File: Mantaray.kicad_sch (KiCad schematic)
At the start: 0 parts

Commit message: External I/O
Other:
- sheet AUDIO OUT ports: added AUDIO_L_OUT, AUDIO_R_OUT, {I2S}; removed none
- sheet External Connectors ports: added AUDIO_L_OUT, AUDIO_R_OUT, AV_MODE0, AV_MODE1, AV_MODE2, EXPPORT_PORT1{USB}, EXPPORT_PORT2{USB}, EXPPORT_PORT3{USB}, EXPPORT_PORT4{USB}, SCART_RGB, SPDIF_OUT, VID_DACA, VID_DACB, VID_DACC, VID_DACD, VID_HSYNC, VID_VSYNC, WSS_CNTL0, WSS_CNTL1, {ETHERNET}, {HDMI}; removed none
- note added: "TODO: - Power Delivery - Audio Out - NAND/eMMC - Replace generic components with real part numbers"
- note removed: "TODO: - Power Delivery - Audio Out - NAND/eMMC - Replace generic components with real part numbers - Also memory i forgot"

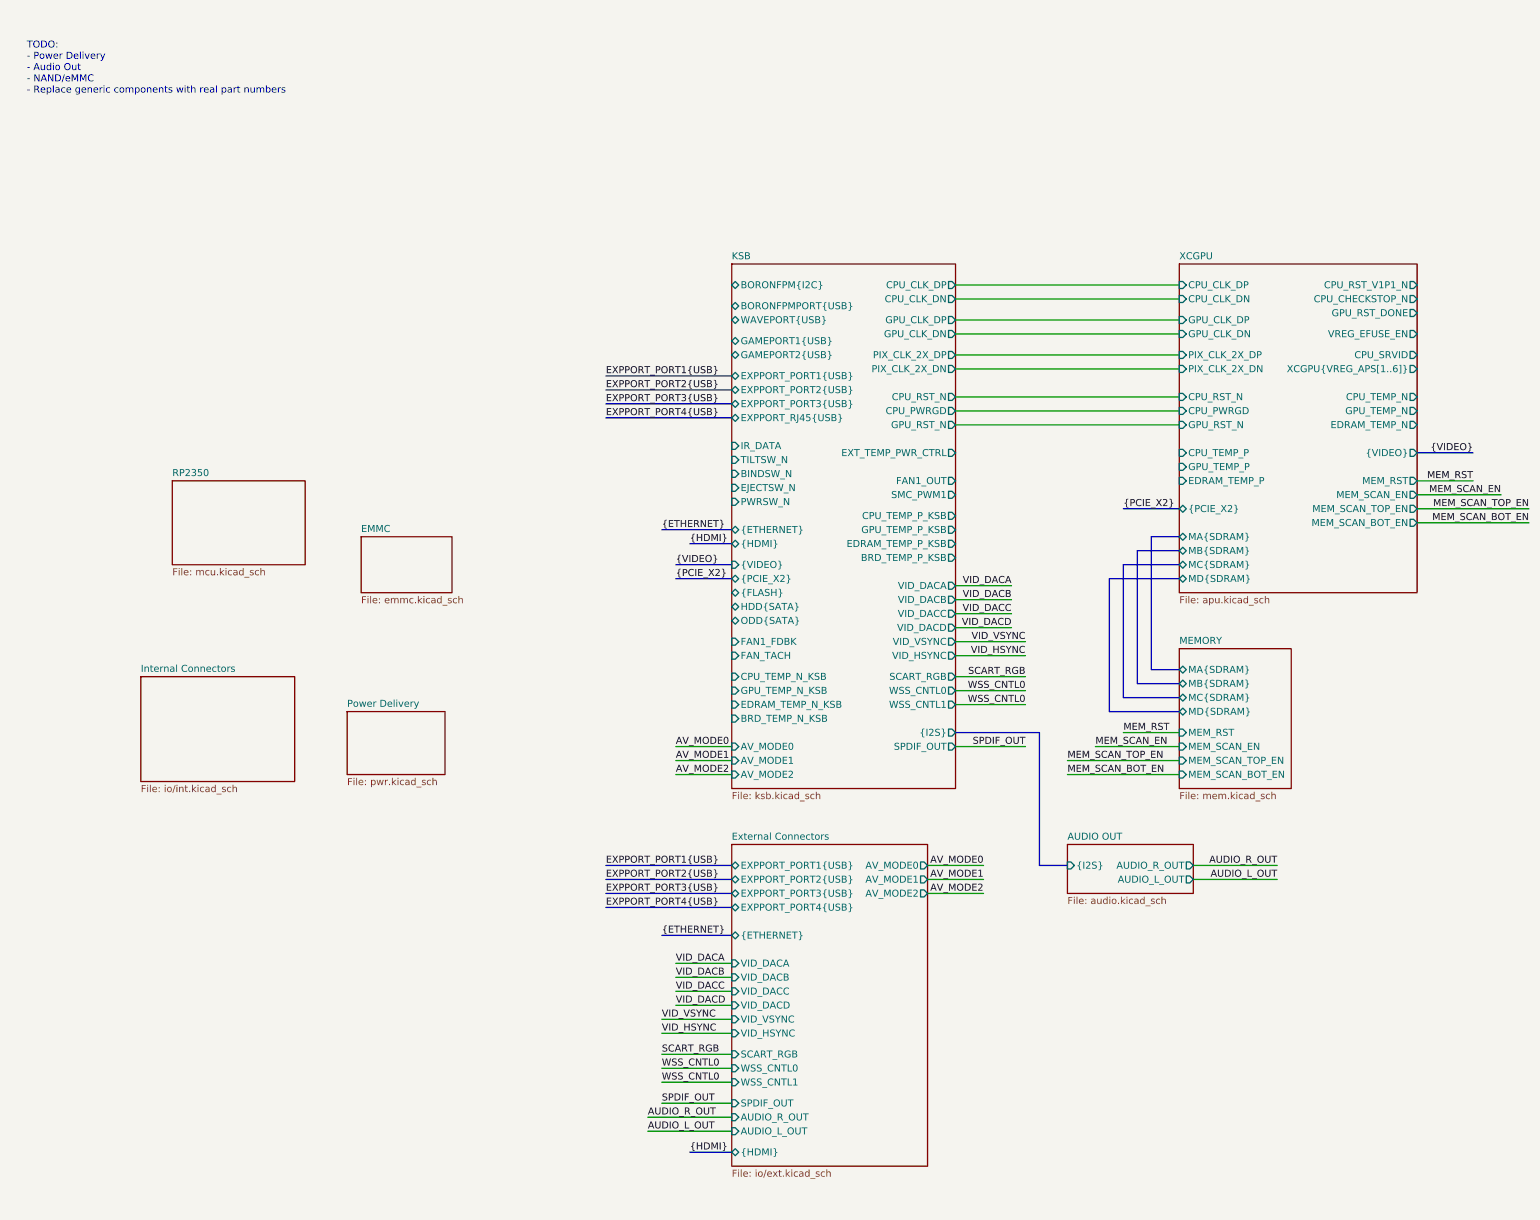
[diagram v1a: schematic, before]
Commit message: Cleanup, SMC GPIO connections and Temperature sensing
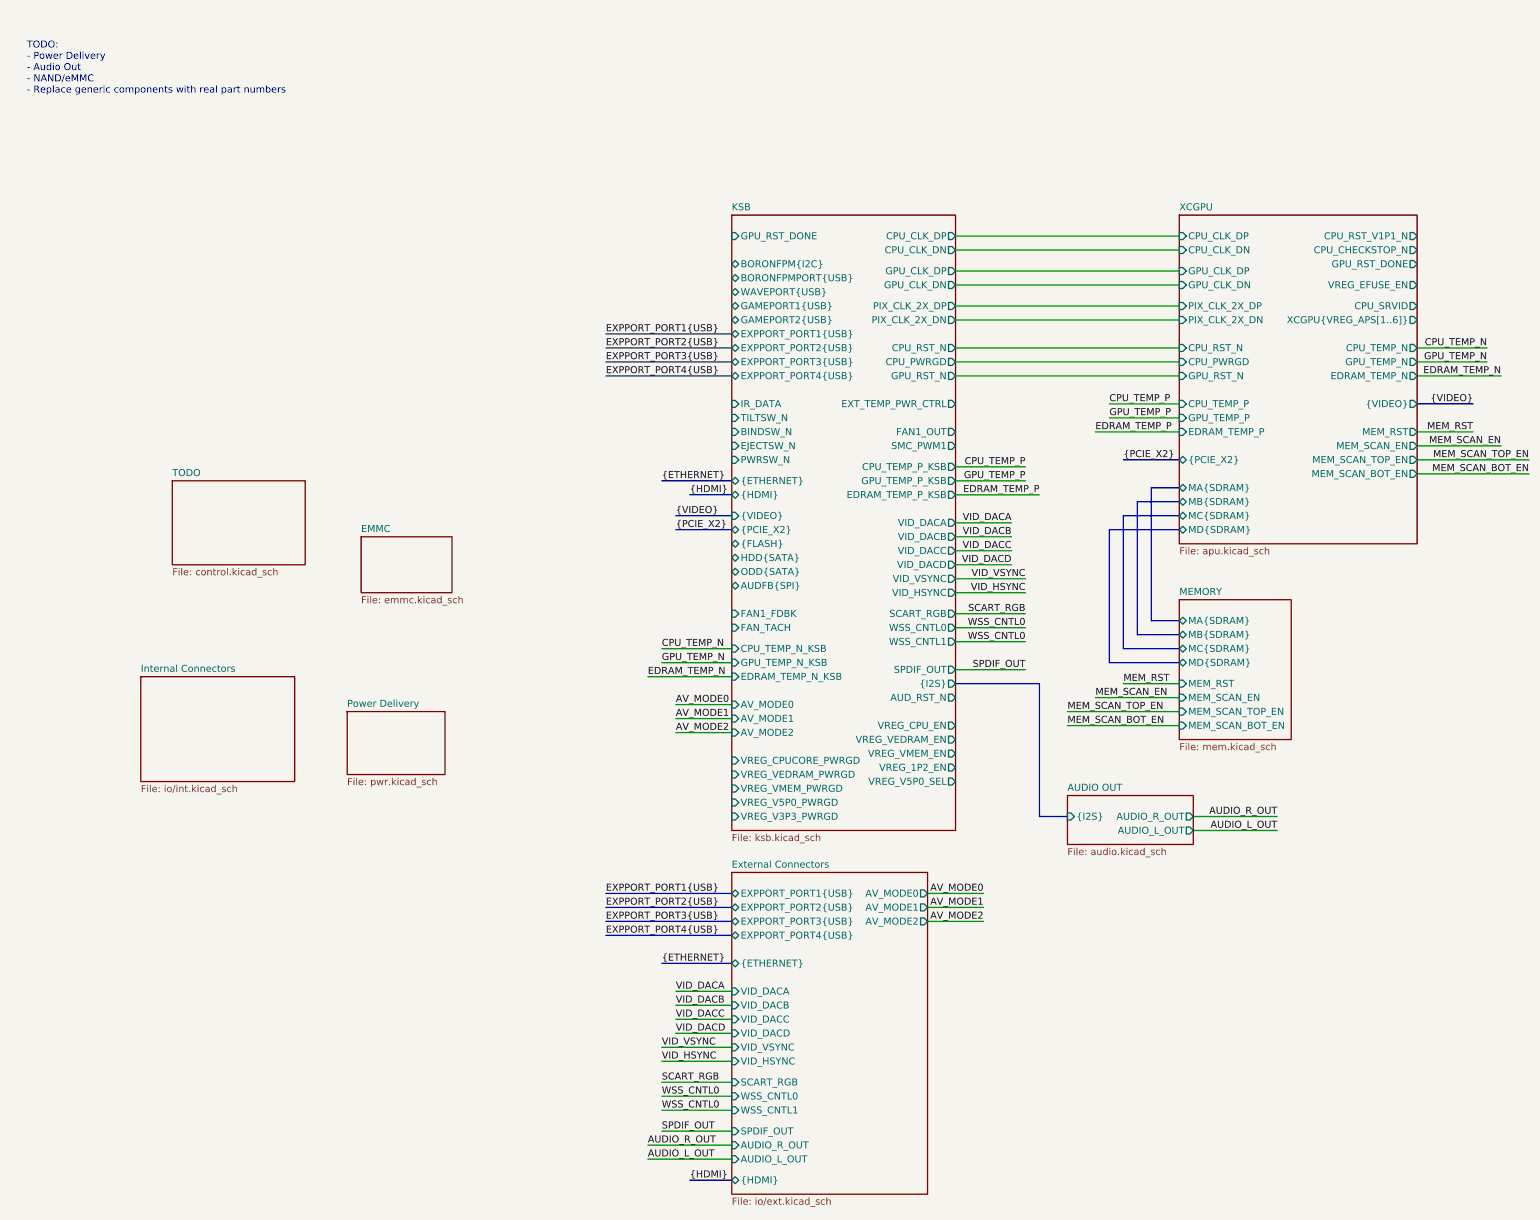
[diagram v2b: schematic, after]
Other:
- sheet RP2350 renamed TODO
- sheet KSB ports: added AUDFB{SPI}, AUD_RST_N, EXPPORT_PORT4{USB}, GPU_RST_DONE, VREG_1P2_EN, VREG_CPUCORE_PWRGD, VREG_CPU_EN, VREG_V3P3_PWRGD, VREG_V5P0_PWRGD, VREG_V5P0_SEL, VREG_VEDRAM_EN, VREG_VEDRAM_PWRGD, VREG_VMEM_EN, VREG_VMEM_PWRGD; removed BRD_TEMP_N_KSB, BRD_TEMP_P_KSB, EXPPORT_RJ45{USB}
- sheet TODO: file mcu.kicad_sch -> control.kicad_sch

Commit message: Internal Connectors
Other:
- sheet External Connectors ports: added EXPPORT_PORT0{USB}; removed EXPPORT_PORT4{USB}
- sheet Internal Connectors ports: added BINDSW_N, BORONFPMPORT{USB}, BORONFPM{I2C}, EJECTSW_N, FAN1_FDBK, FAN1_OUT, FAN_TACH, GAMEPORT1{USB}, GAMEPORT2{USB}, IR_DATA, PWRSW_N, SMC_PWM1, SPKR_DRIVE_N, SPKR_DRIVE_P, TILTSW_N, TRAY_OPEN, TRAY_STATUS; removed none
- sheet KSB ports: added EXPPORT_PORT0{USB}, TRAY_OPEN, TRAY_STATUS; removed EXPPORT_PORT4{USB}, EXT_TEMP_PWR_CTRL

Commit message: Cleanup & Debug I/O
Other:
- sheet EMMC renamed FLASH
- removed sheet TODO
- sheet AUDIO OUT ports: added AUD_RST_N; removed none
- sheet FLASH: file emmc.kicad_sch -> flash.kicad_sch
- sheet FLASH ports: added {FLASH}; removed none
- sheet Power Delivery ports: added ATX_PWRGD, PWR_EN; removed none
- note added: "Board Jumpers: - JP1: CPU Debug Enable - JP2: GPU Debug Enable - JP3: - JP4: External ROM Enable - JP5 - JP6: SMC Debug Mode"
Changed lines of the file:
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@@
 		(members "PIX_DATA[0..14]" "PIX_CLK" "VSYNC_OUT" "HSYNC_OUT")
 	)
+	(text "Board Jumpers:\n- JP1: CPU Debug Enable\n- JP2: GPU Debug Enable\n- JP3:\n- JP4: External ROM Enable\n- JP5\n- JP6: SMC Debug Mode"
+		(exclude_from_sim no)
+		(at 19.05 23.622 0)
+		(effects
+			(font
+				(size 1.27 1.27)
+			)
+			(justify left)
+		)
+	)
 	(text "TODO:\n- Power Delivery\n- Audio Out\n- NAND/eMMC\n- Replace generic components with real part numbers\n"
 		(exclude_from_sim no)
@@
 	(wire
 		(pts
+			(xy 172.72 134.62) (xy 180.34 134.62)
+		)
+		(stroke
+			(width 0)
+			(type default)
+		)
+	)
+	(wire
+		(pts
 			(xy 162.56 170.18) (xy 152.4 170.18)
 		)
@@
 	(wire
 		(pts
+			(xy 172.72 111.76) (xy 172.72 134.62)
+		)
+		(stroke
+			(width 0)
+			(type default)
+		)
+	)
+	(wire
+		(pts
 			(xy 106.68 69.85) (xy 116.84 69.85)
 		)
@@
 	(wire
 		(pts
+			(xy 160.02 111.76) (xy 172.72 111.76)
+		)
+		(stroke
+			(width 0)
+			(type default)
+		)
+	)
+	(wire
+		(pts
 			(xy 44.45 166.37) (xy 31.75 166.37)
 		)
@@
 	(wire
 		(pts
-			(xy 203.2 134.62) (xy 218.44 134.62)
+			(xy 208.28 134.62) (xy 223.52 134.62)
 		)
 		(stroke
@@
 	(wire
 		(pts
-			(xy 203.2 132.08) (xy 218.44 132.08)
+			(xy 208.28 132.08) (xy 223.52 132.08)
 		)
 		(stroke
@@
 	)
 	(label "AUDIO_L_OUT"
-		(at 218.44 134.62 180)
+		(at 223.52 134.62 180)
 		(effects
 			(font
@@
 	)
 	(label "AUDIO_R_OUT"
-		(at 218.44 132.08 180)
+		(at 223.52 132.08 180)
 		(effects
 			(font
@@
 	(sheet
 		(at 180.34 128.27)
-		(size 22.86 8.89)
+		(size 27.94 8.89)
 		(exclude_from_sim no)
 		(in_bom yes)
@@
 		)
 		(pin "AUDIO_L_OUT" output
-			(at 203.2 134.62 0)
+			(at 208.28 134.62 0)
 			(effects
 				(font
@@
 		)
 		(pin "AUDIO_R_OUT" output
-			(at 203.2 132.08 0)
+			(at 208.28 132.08 0)
 			(effects
 				(font
@@
 			)
 		)
+		(pin "AUD_RST_N" input
+			(at 180.34 134.62 180)
+			(effects
+				(font
+					(size 1.27 1.27)
+				)
+				(justify left)
+			)
+		)
 		(instances
 			(project "Mantaray"
@@
 	)
 	(sheet
-		(at 39.37 80.01)
-		(size 17.78 11.43)
+		(at 38.1 80.01)
+		(size 22.86 11.43)
 		(exclude_from_sim no)
 		(in_bom yes)
@@
 		)
 		(property "Sheetname" "Power Delivery"
-			(at 39.37 79.2984 0)
+			(at 38.1 79.2984 0)
 			(effects
 				(font
@@
 		)
 		(property "Sheetfile" "pwr.kicad_sch"
-			(at 39.37 92.0246 0)
+			(at 38.1 92.0246 0)
 			(effects
 				(font
@@
 			)
 		)
+		(pin "ATX_PWRGD" output
+			(at 60.96 83.82 0)
+			(effects
+				(font
+					(size 1.27 1.27)
+				)
+				(justify right)
+			)
+		)
+		(pin "PWR_EN" input
+			(at 38.1 83.82 180)
+			(effects
+				(font
+					(size 1.27 1.27)
+				)
+				(justify left)
+			)
+		)
 		(instances
 			(project "Mantaray"
@@
 			(color 0 0 0 0.0000)
 		)
-		(property "Sheetname" "EMMC"
+		(property "Sheetname" "FLASH"
 			(at 41.91 47.5484 0)
 			(effects
@@
 			)
 		)
-		(property "Sheetfile" "emmc.kicad_sch"
+		(property "Sheetfile" "flash.kicad_sch"
 			(at 41.91 59.0046 0)
 			(effects
@@
 			)
 		)
+		(pin "{FLASH}" bidirectional
+			(at 41.91 52.07 180)
+			(effects
+				(font
+					(size 1.27 1.27)
+				)
+				(justify left)
+			)
+		)
 		(instances
 			(project "Mantaray"
@@
 				)
 			)
-		)
-	)
-	(sheet
-		(at -1.27 -17.78)
-		(size 62.23 15.24)
-		(exclude_from_sim no)
-		(in_bom yes)
-		(on_board yes)
-		(dnp no)
-		(fields_autoplaced yes)
-		(stroke
-			(width 0.1524)
-			(type solid)
-		)
-		(fill
-			(color 0 0 0 0.0000)
-		)
-		(property "Sheetname" "TODO"
-			(at -1.27 -18.4916 0)
-			(effects
-				(font
-					(size 1.27 1.27)
-				)
-				(justify left bottom)
-			)
-		)
-		(property "Sheetfile" "control.kicad_sch"
-			(at -1.27 -1.9554 0)
-			(effects
-				(font
-					(size 1.27 1.27)
-				)
-				(justify left top)
-			)
-		)
-		(instances
-			(project "Mantaray"
-				(path "/16640ecb-e4a4-4594-871b-70047bfba6e0"
-					(page "22")
-				)
-			)

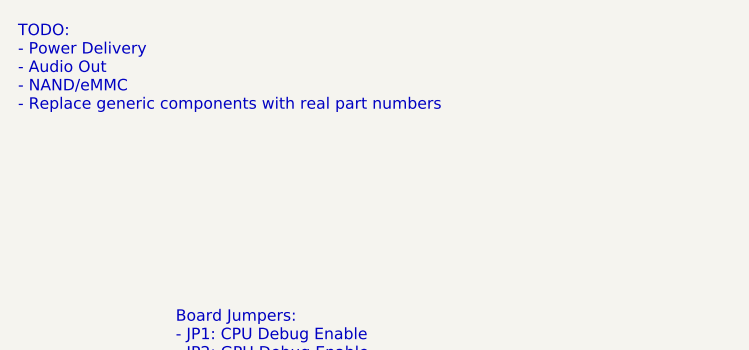
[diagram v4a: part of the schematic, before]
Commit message: Audio Output, Analog isolation and TOSLINK
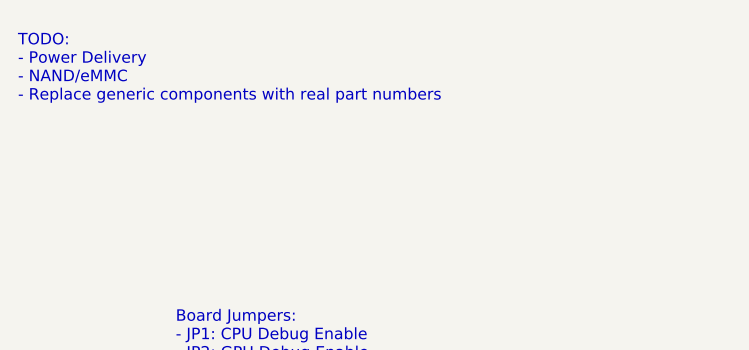
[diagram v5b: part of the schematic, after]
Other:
- note added: "TODO: - Power Delivery - NAND/eMMC - Replace generic components with real part numbers"
- note removed: "TODO: - Power Delivery - Audio Out - NAND/eMMC - Replace generic components with real part numbers"
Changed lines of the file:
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@@
 		)
 	)
-	(text "TODO:\n- Power Delivery\n- Audio Out\n- NAND/eMMC\n- Replace generic components with real part numbers\n"
+	(text "TODO:\n- Power Delivery\n- NAND/eMMC\n- Replace generic components with real part numbers\n"
 		(exclude_from_sim no)
 		(at 1.524 -10.16 0)

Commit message: Debug Connectors
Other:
- added sheet Debug Connectors (io/debug.kicad_sch)
